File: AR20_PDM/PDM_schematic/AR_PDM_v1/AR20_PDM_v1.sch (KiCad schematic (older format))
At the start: 2 parts

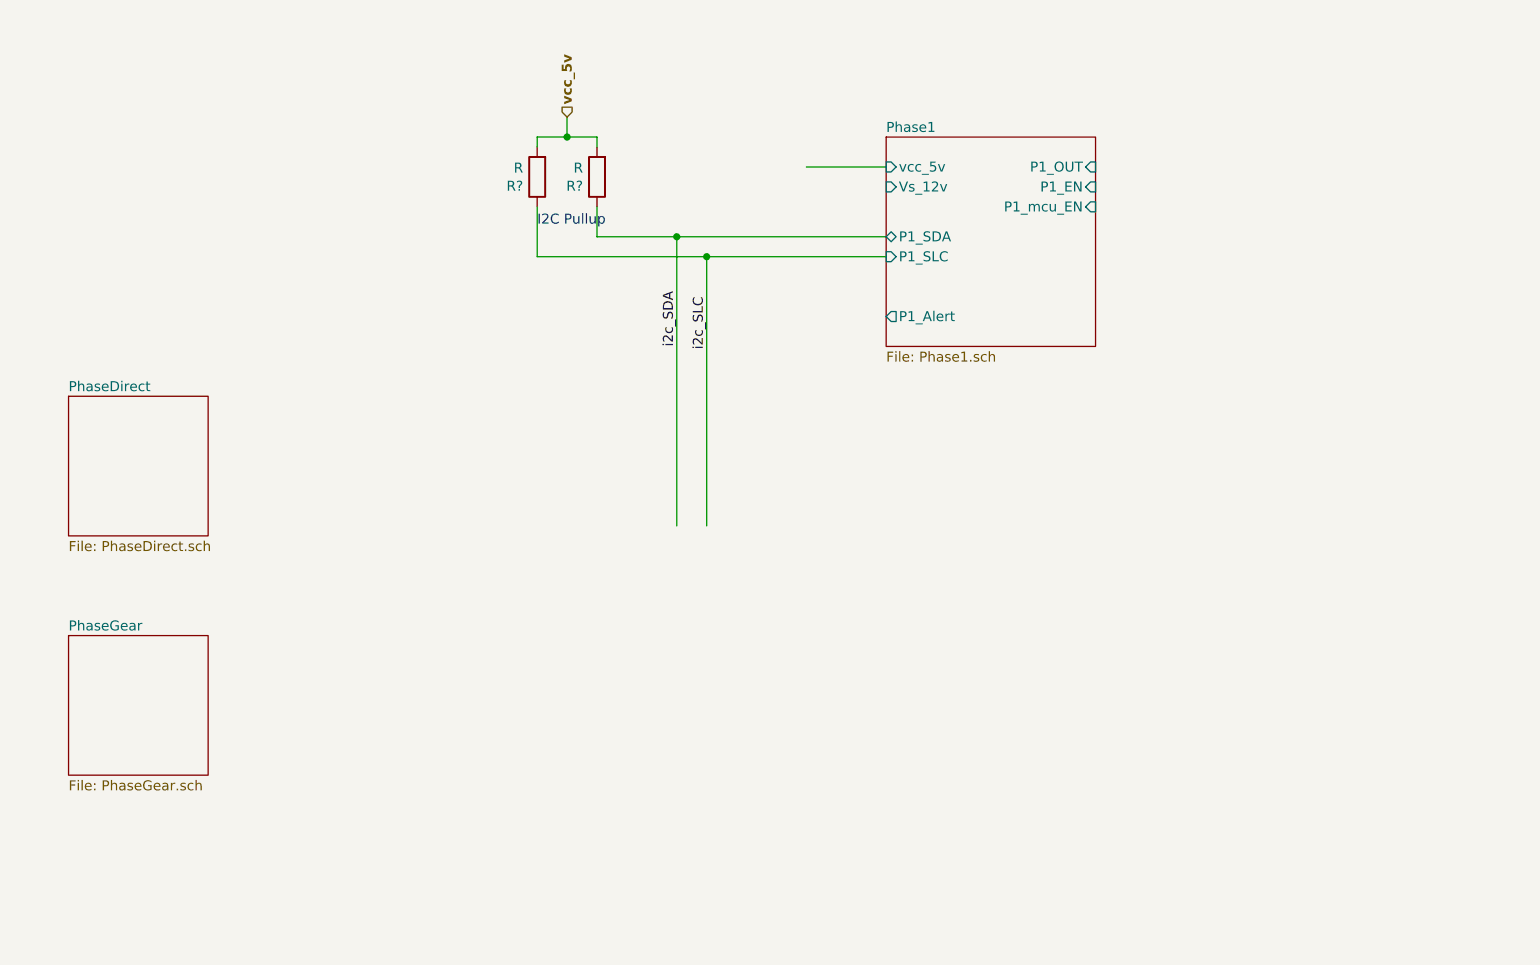
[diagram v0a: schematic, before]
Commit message: First draft of Gear phase, shutdown relays, and Direct phases.
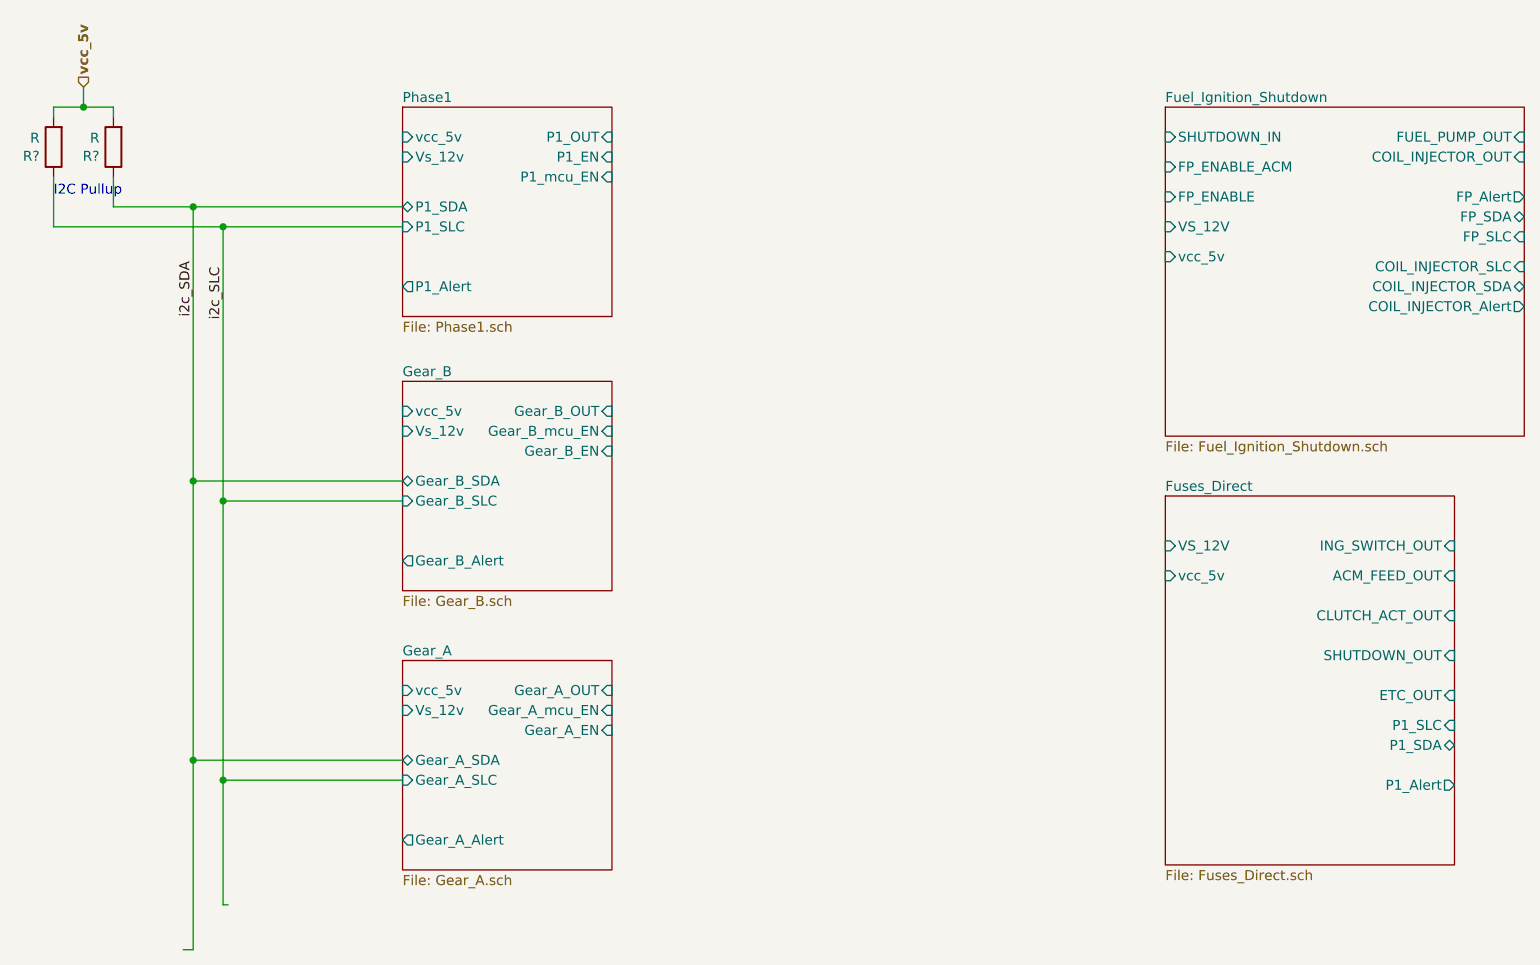
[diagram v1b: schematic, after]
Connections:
- wire segments 14 -> 23
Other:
- moved on the sheet: R?
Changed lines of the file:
@@
 $Descr A4 11693 8268
 encoding utf-8
-Sheet 1 4
+Sheet 1 6
 Title ""
 Date ""
@@
 Comment4 ""
 $EndDescr
-Wire Wire Line
-	5450 1300 5050 1300
-$Sheet
-S 1350 2450 700  700
-U 5DA8920B
-F0 "PhaseDirect" 50
-F1 "PhaseDirect.sch" 50
-$EndSheet
-$Sheet
-S 1350 3650 700  700
-U 5DA89204
-F0 "PhaseGear" 50
-F1 "PhaseGear.sch" 50
-$EndSheet
-Wire Wire Line
-	5450 1650 4400 1650
-Wire Wire Line
-	4400 1650 4400 3100
-Wire Wire Line
-	5450 1750 4550 1750
-Wire Wire Line
-	4550 1750 4550 3100
-Text Label 4400 2200 1    50   ~ 0
+Text Label 1975 2050 1    50   ~ 0
 i2c_SDA
-Text Label 4550 1950 3    50   ~ 0
+Text Label 2125 1800 3    50   ~ 0
 i2c_SLC
 $Comp
 L AR20_PDM_v1-rescue:R-Device R?
 U 1 1 5DAD398E
-P 4000 1350
+P 1575 1200
 AR Path="/5DA89415/5DAD398E" Ref="R?"  Part="1"
 AR Path="/5DAD398E" Ref="R?"  Part="1"
-F 0 "R?" H 4070 1396 50  0000 L CNN
-F 1 "R" H 4070 1305 50  0000 L CNN
-F 2 "" V 3930 1350 50  0001 C CNN
-F 3 "~" H 4000 1350 50  0001 C CNN
-	1    4000 1350
+F 0 "R?" H 1645 1246 50  0000 L CNN
+F 1 "R" H 1645 1155 50  0000 L CNN
+F 2 "" V 1505 1200 50  0001 C CNN
+F 3 "~" H 1575 1200 50  0001 C CNN
+	1    1575 1200
 	-1   0    0    1
 $EndComp
@@
 L AR20_PDM_v1-rescue:R-Device R?
 U 1 1 5DAD3BC1
-P 3700 1350
+P 1275 1200
 AR Path="/5DA89415/5DAD3BC1" Ref="R?"  Part="1"
 AR Path="/5DAD3BC1" Ref="R?"  Part="1"
-F 0 "R?" H 3770 1396 50  0000 L CNN
-F 1 "R" H 3770 1305 50  0000 L CNN
-F 2 "" V 3630 1350 50  0001 C CNN
-F 3 "~" H 3700 1350 50  0001 C CNN
-	1    3700 1350
+F 0 "R?" H 1345 1246 50  0000 L CNN
+F 1 "R" H 1345 1155 50  0000 L CNN
+F 2 "" V 1205 1200 50  0001 C CNN
+F 3 "~" H 1275 1200 50  0001 C CNN
+	1    1275 1200
 	-1   0    0    1
 $EndComp
 Wire Wire Line
-	4400 1650 4000 1650
+	1575 1350 1575 1500
 Wire Wire Line
-	4000 1500 4000 1650
-Connection ~ 4400 1650
+	1275 1600 1275 1350
 Wire Wire Line
-	4550 1750 3700 1750
+	1575 1050 1575 1000
 Wire Wire Line
-	3700 1750 3700 1500
-Connection ~ 4550 1750
+	1575 1000 1425 1000
 Wire Wire Line
-	4000 1200 4000 1150
+	1275 1000 1275 1050
 Wire Wire Line
-	4000 1150 3850 1150
+	1425 1000 1425 900
+Connection ~ 1425 1000
 Wire Wire Line
-	3700 1150 3700 1200
-Wire Wire Line
-	3850 1150 3850 1050
-Connection ~ 3850 1150
-Wire Wire Line
-	3850 1150 3700 1150
-Text HLabel 3850 1050 1    50   Input ~ 10
+	1425 1000 1275 1000
+Text HLabel 1425 900  1    50   Input ~ 10
 vcc_5v
-Text Notes 3700 1600 0    50   ~ 0
+Text Notes 1275 1450 0    50   ~ 0
 I2C Pullup
 $Sheet
-S 5450 1150 1050 1050
+S 3025 1000 1050 1050
 U 5DA89415
 F0 "Phase1" 50
 F1 "Phase1.sch" 50
-F2 "Vs_12v" I L 5450 1400 50
-F3 "vcc_5v" I L 5450 1300 50
-F4 "P1_SDA" B L 5450 1650 50
-F5 "P1_SLC" I L 5450 1750 50
-F6 "P1_OUT" I R 6500 1300 50
-F7 "P1_Alert" O L 5450 2050 50
-F8 "P1_EN" I R 6500 1400 50
-F9 "P1_mcu_EN" I R 6500 1500 50
+F2 "Vs_12v" I L 3025 1250 50
+F3 "vcc_5v" I L 3025 1150 50
+F4 "P1_SDA" B L 3025 1500 50
+F5 "P1_SLC" I L 3025 1600 50
+F6 "P1_OUT" I R 4075 1150 50
+F7 "P1_Alert" O L 3025 1900 50
+F8 "P1_EN" I R 4075 1250 50
+F9 "P1_mcu_EN" I R 4075 1350 50
 $EndSheet
+$Sheet
+S 6850 2950 1450 1850
+U 5DE4D361
+F0 "Fuses_Direct" 50
+F1 "Fuses_Direct.sch" 50
+F2 "ING_SWITCH_OUT" I R 8300 3200 50
+F3 "ACM_FEED_OUT" I R 8300 3350 50
+F4 "CLUTCH_ACT_OUT" I R 8300 3550 50
+F5 "SHUTDOWN_OUT" I R 8300 3750 50
+F6 "ETC_OUT" I R 8300 3950 50
+F7 "P1_SLC" I R 8300 4100 50
+F8 "P1_SDA" B R 8300 4200 50
+F9 "P1_Alert" O R 8300 4400 50
+F10 "vcc_5v" I L 6850 3350 50
+F11 "VS_12V" I L 6850 3200 50
+$EndSheet
+$Sheet
+S 6850 1000 1800 1650
+U 5DA8920B
+F0 "Fuel_Ignition_Shutdown" 50
+F1 "Fuel_Ignition_Shutdown.sch" 50
+F2 "FUEL_PUMP_OUT" I R 8650 1150 50
+F3 "SHUTDOWN_IN" I L 6850 1150 50
+F4 "FP_ENABLE_ACM" I L 6850 1300 50
+F5 "FP_ENABLE" I L 6850 1450 50
+F6 "COIL_INJECTOR_OUT" I R 8650 1250 50
+F7 "VS_12V" I L 6850 1600 50
+F8 "vcc_5v" I L 6850 1750 50
+F9 "FP_Alert" O R 8650 1450 50
+F10 "FP_SDA" B R 8650 1550 50
+F11 "FP_SLC" I R 8650 1650 50
+F12 "COIL_INJECTOR_SLC" I R 8650 1800 50
+F13 "COIL_INJECTOR_SDA" B R 8650 1900 50
+F14 "COIL_INJECTOR_Alert" O R 8650 2000 50
+$EndSheet
+Wire Wire Line
+	2125 1600 1275 1600
+Wire Wire Line
+	3025 1600 2125 1600
+Connection ~ 2125 1600
+Wire Wire Line
+	1975 1500 1575 1500
+Wire Wire Line
+	3025 1500 1975 1500
+Connection ~ 1975 1500
+$Sheet
+S 3025 2375 1050 1050
+U 5DEB10A1
+F0 "Gear_B" 50
+F1 "Gear_B.sch" 50
+F2 "Vs_12v" I L 3025 2625 50
+F3 "vcc_5v" I L 3025 2525 50
+F4 "Gear_B_Alert" O L 3025 3275 50
+F5 "Gear_B_SDA" B L 3025 2875 50
+F6 "Gear_B_SLC" I L 3025 2975 50
+F7 "Gear_B_OUT" I R 4075 2525 50
+F8 "Gear_B_mcu_EN" I R 4075 2625 50
+F9 "Gear_B_EN" I R 4075 2725 50
+$EndSheet
+$Sheet
+S 3025 3775 1050 1050
+U 5DEB20EA
+F0 "Gear_A" 50
+F1 "Gear_A.sch" 50
+F2 "Vs_12v" I L 3025 4025 50
+F3 "vcc_5v" I L 3025 3925 50
+F4 "Gear_A_Alert" O L 3025 4675 50
+F5 "Gear_A_SDA" B L 3025 4275 50
+F6 "Gear_A_SLC" I L 3025 4375 50
+F7 "Gear_A_OUT" I R 4075 3925 50
+F8 "Gear_A_mcu_EN" I R 4075 4025 50
+F9 "Gear_A_EN" I R 4075 4125 50
+$EndSheet
+Wire Wire Line
+	3025 2875 1975 2875
+Wire Wire Line
+	1975 1500 1975 2875
+Connection ~ 1975 2875
+Wire Wire Line
+	3025 2975 2125 2975
+Wire Wire Line
+	2125 1600 2125 2975
+Wire Wire Line
+	2125 2975 2125 4375
+Wire Wire Line
+	2125 5000 2150 5000
+Connection ~ 2125 2975
+Wire Wire Line
+	1975 5225 1925 5225
+Wire Wire Line
+	3025 4275 1975 4275
+Wire Wire Line
+	1975 2875 1975 4275
+Connection ~ 1975 4275
+Wire Wire Line
+	1975 4275 1975 5225
+Wire Wire Line
+	3025 4375 2125 4375
+Connection ~ 2125 4375
+Wire Wire Line
+	2125 4375 2125 5000
 $EndSCHEMATC

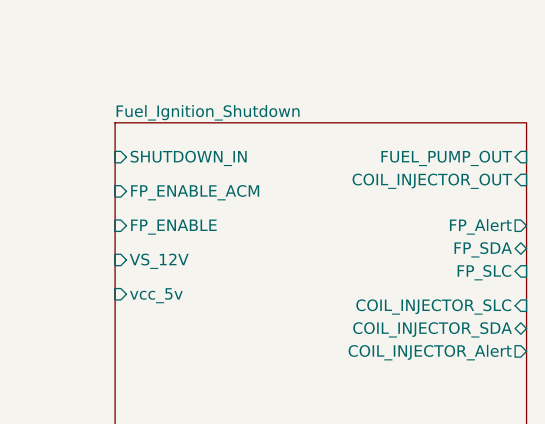
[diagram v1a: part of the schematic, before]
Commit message: Added label on mosfets, added fuel pump sinking output
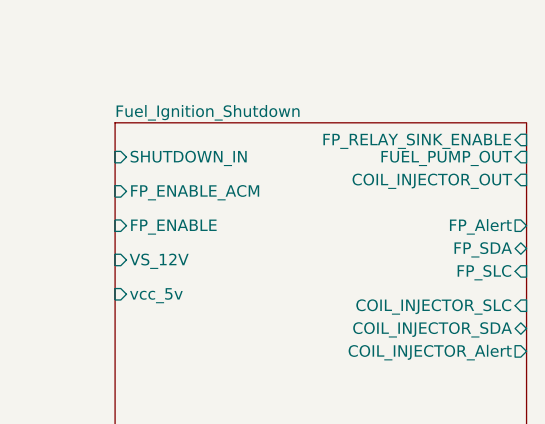
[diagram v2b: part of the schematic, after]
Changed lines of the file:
@@
 F13 "COIL_INJECTOR_SDA" B R 8650 1900 50
 F14 "COIL_INJECTOR_Alert" O R 8650 2000 50
+F15 "FP_RELAY_SINK_ENABLE" I R 8650 1075 50
 $EndSheet
 Wire Wire Line

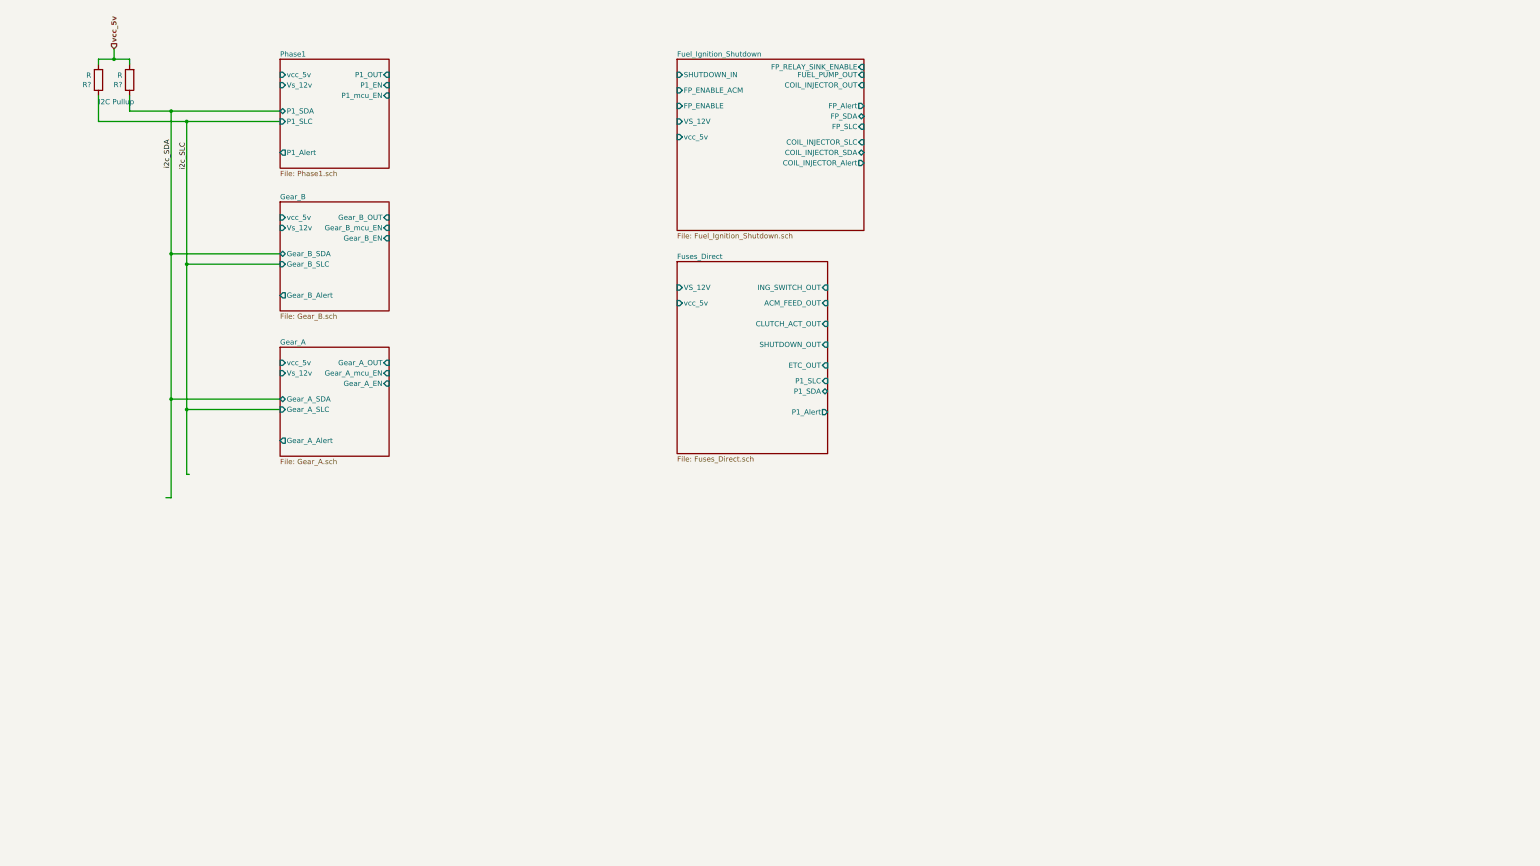
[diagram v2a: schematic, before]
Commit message: Major Schematics changes-work in progress
- Added rest of the phases
- Corrected pin names, and began to connect everything
- Began mapping the connectors, Pin-out not yet verified for all connectors
- Began mapping of user interface (Led indicators)
- INA233 now senses OUT voltage on mosfets instead of main 12Volt
- Added extra decoupling capacitors
Known things to fix:
- AUX inputs activation method, and a disconnect switch on phase 1-7 (mosfets)
- Rest of the user interface
- Find correct plugs for the system
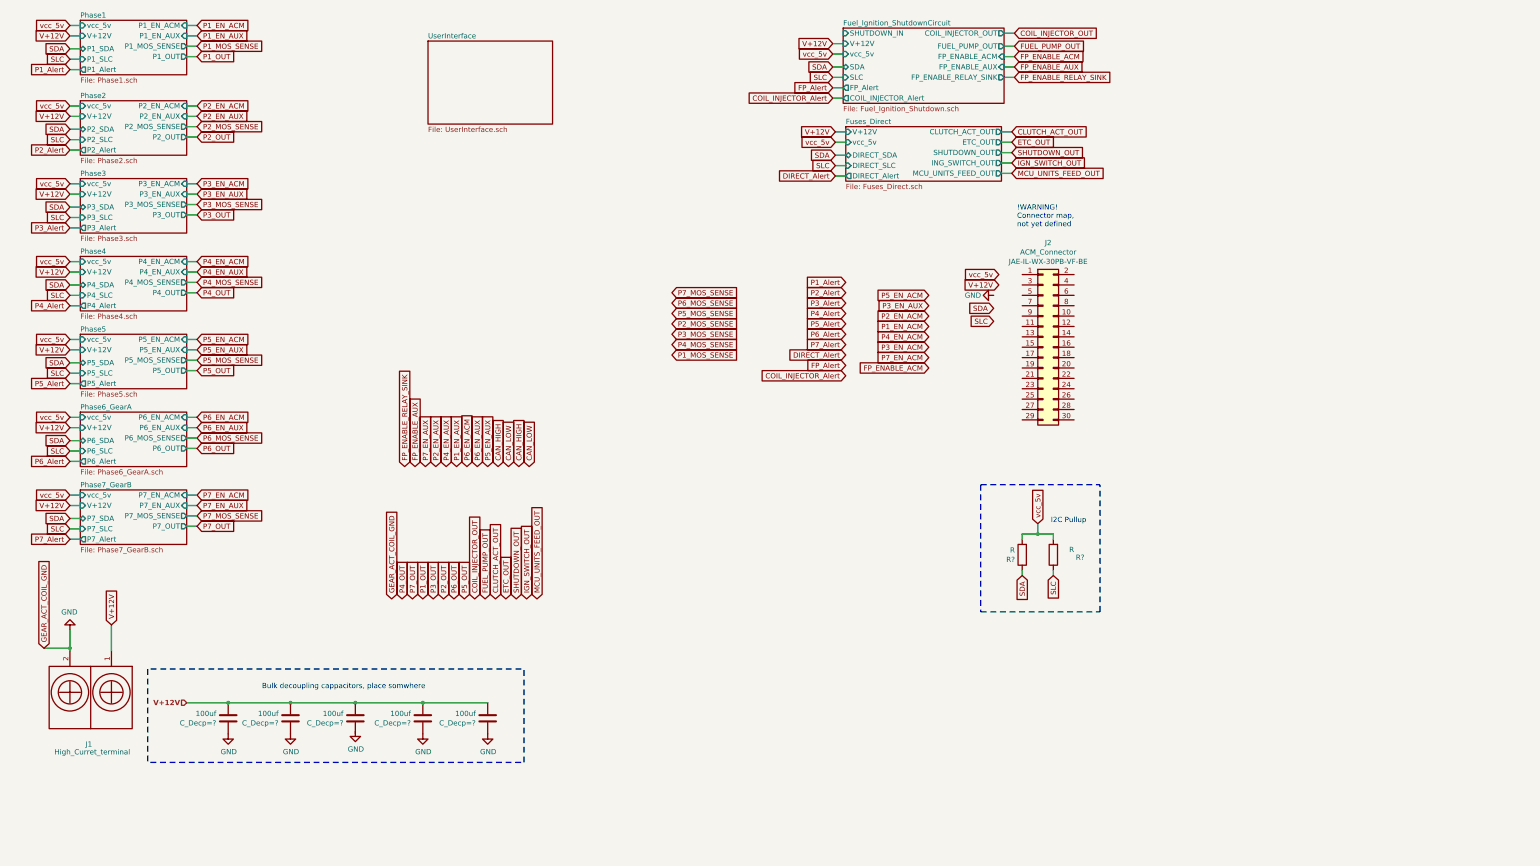
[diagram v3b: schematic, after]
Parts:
- added C_Decp=? (x5): 100uf, symbol AR20_PDM_v1-rescue:C-Device
- added J1: High_Curret_terminal, symbol AR20_PDM_v1-rescue:High_Curret_terminal
- added J2: ACM_Connector, symbol Connector_Generic:Conn_02x15_Odd_Even
- gave numbers to parts that had none: 1
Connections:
- net labels added: CAN_HIGH, CAN_LOW, CLUTCH_ACT_OUT, COIL_INJECTOR_Alert, COIL_INJECTOR_OUT, DIRECT_Alert, ETC_OUT, FP_Alert, FP_ENABLE_ACM, FP_ENABLE_AUX, FP_ENABLE_RELAY_SINK, FUEL_PUMP_OUT, GEAR_ACT_COIL_GND, GND, IGN_SWITCH_OUT, MCU_UNITS_FEED_OUT, P1_Alert, P1_EN_ACM, P1_EN_AUX, P1_MOS_SENSE, P1_OUT, P2_Alert, P2_EN_ACM, P2_EN_AUX, P2_MOS_SENSE, P2_OUT, P3_Alert, P3_EN_ACM, P3_EN_AUX, P3_MOS_SENSE, P3_OUT, P4_Alert, P4_EN_ACM, P4_EN_AUX, P4_MOS_SENSE, P4_OUT, P5_Alert, P5_EN_ACM, P5_EN_AUX, P5_MOS_SENSE, P5_OUT, P6_Alert, P6_EN_ACM, P6_EN_AUX, P6_MOS_SENSE, P6_OUT, P7_Alert, P7_EN_ACM, P7_EN_AUX, P7_MOS_SENSE, P7_OUT, SDA, SHUTDOWN_OUT, SLC, V+12V
- net labels removed: i2c_SDA, i2c_SLC
- wire segments 23 -> 100
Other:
- note added: "!WARNING!\nConnector map,\nnot yet defined"
- note added: "Bulk decoupling cappacitors, place somwhere"
- moved on the sheet: R?
